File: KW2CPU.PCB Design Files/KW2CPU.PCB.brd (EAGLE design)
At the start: 44 x 30 mm, 75 parts, among them IC1 25AA080SN, J1 DF12_M, U1 MKW21D, U3 RF6555, U4 3.3V, X1 32.768kHz, X2 32MHZ

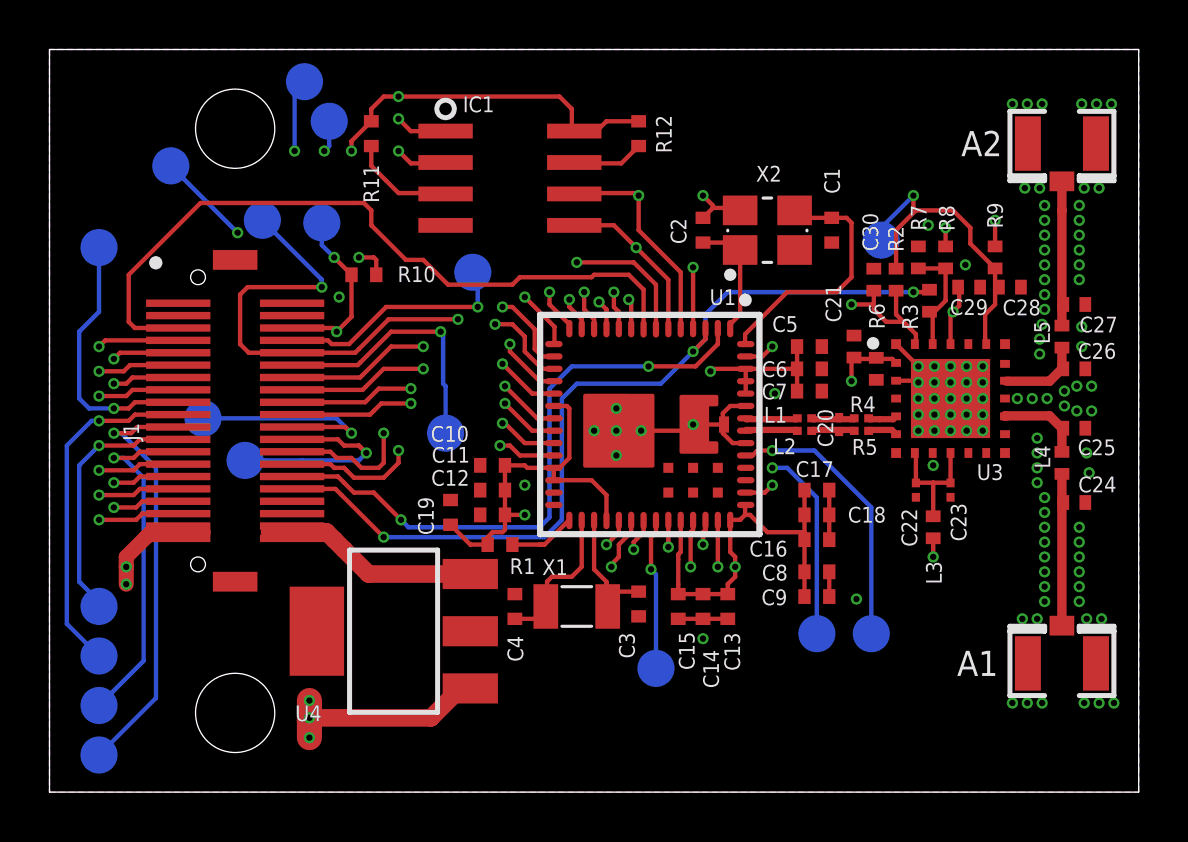
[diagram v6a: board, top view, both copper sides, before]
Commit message: Omitted brd file from commit
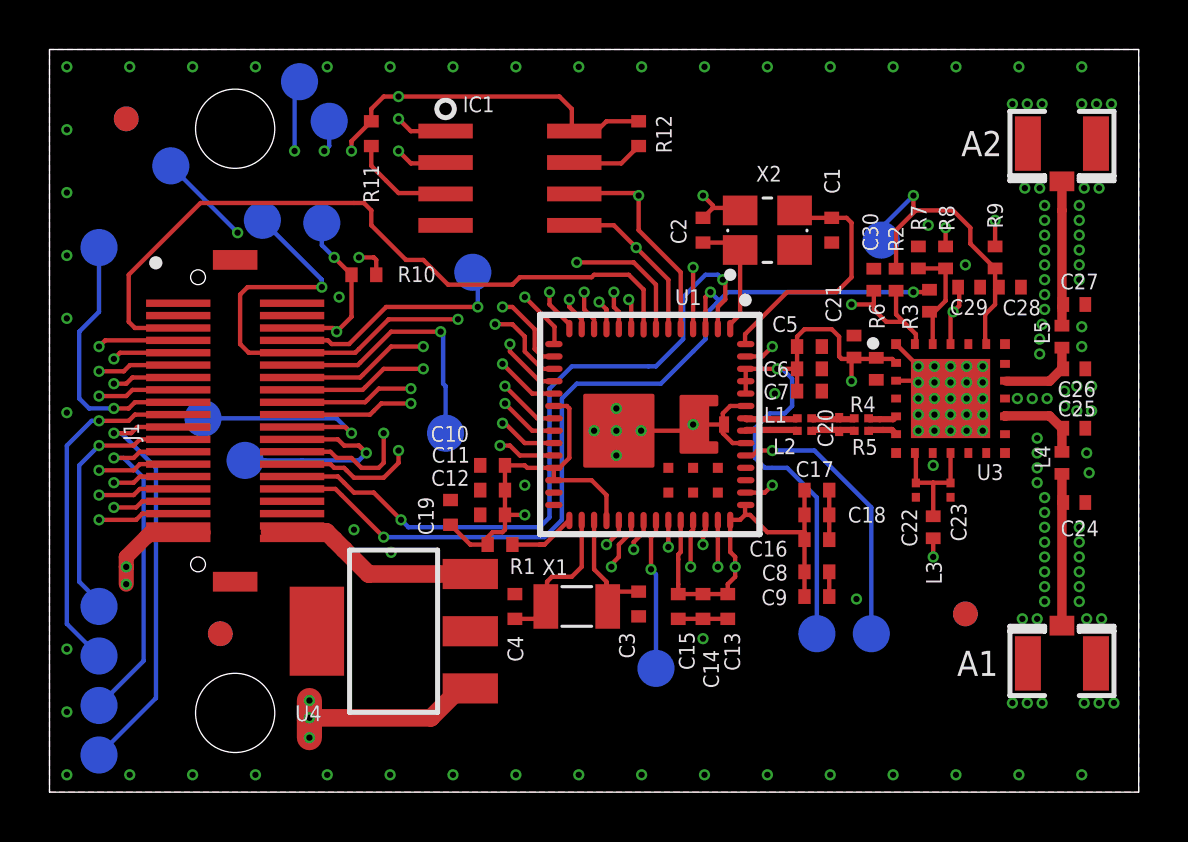
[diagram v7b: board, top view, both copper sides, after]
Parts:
- added U$2, U$3, U$4, U$5, U$6, U$7: FIDUCIAL, adafruit:FIDUCIAL_1MM
- moved TP10 0.20 mm to (1.60, 13.7)
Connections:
- net N$1 renamed !WP
- net N$2 renamed !HOLD
- net N$4 renamed RFN_MATCH
- net N$5 renamed RFP_MATCH
- net N$8 renamed C_LNA
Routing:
- net RADIO_AREG: track 36.4 -> 26.1 mm, vias 3 -> 2
- net GPIO1: track 24.8 -> 28.8 mm
- net GPIO2: track 35.5 -> 36.5 mm
- net GND: vias 108 -> 151
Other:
- board text added: "8/11/15"
- board text removed: "8/5/15"
- board text removed: "JTAG"
